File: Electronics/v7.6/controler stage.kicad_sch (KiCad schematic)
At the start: 26 parts, among them IC4 RTC PCF8523T, J1 Conn_02x03_Odd_Even, SW2 SPST_TACT-KMR2, U1 ATSAMD21G18A, U4 Adafruit LCD Screen, X1 ClockXtal, X2 uXtal, X4 microsd

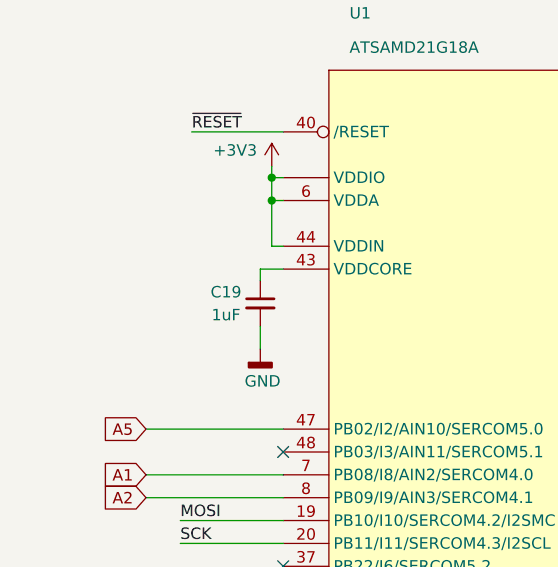
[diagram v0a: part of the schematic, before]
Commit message: Major changes. Check description for more info.
CRITICAL
- Added proper Mask for the battery's GND connection.
- Added 100nF bypass capacitors to microcontroller's VDDIN and VDDA.

IMPROVEMENTS
- Added 100nF capacitor to create a low-pass filter in the battery resistor-divider.
- Improved GND connectivity between USB-C connector and GND planes.
- Added vias on test pads to make it easier/faster to probe.
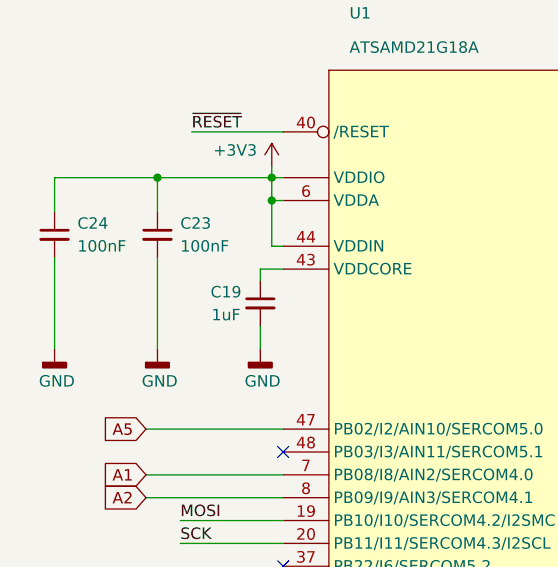
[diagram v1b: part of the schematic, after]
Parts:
- added C23, C24: 100nF, Capacitor_SMD:C_0402_1005Metric, symbol Device:C_Small
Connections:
- net +3V3: now also C23.1, C24.1
- net GND: now also C23.2, C24.2
